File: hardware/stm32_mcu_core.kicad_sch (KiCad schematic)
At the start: 17 parts, among them J4 Conn_ST_STDC14, U5 74AHCT125, U6 STM32G431KBTx, U7 SN74LVC1T45DBV

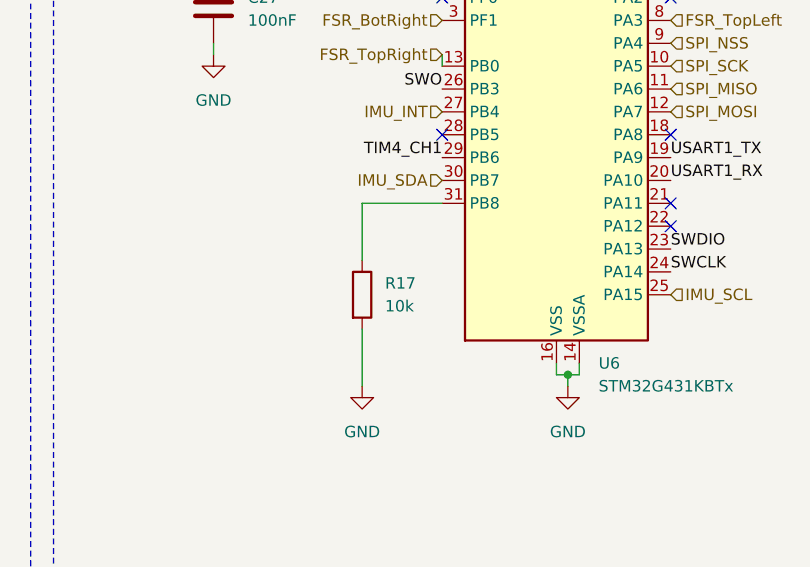
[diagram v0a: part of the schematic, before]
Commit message: Adding power LED status
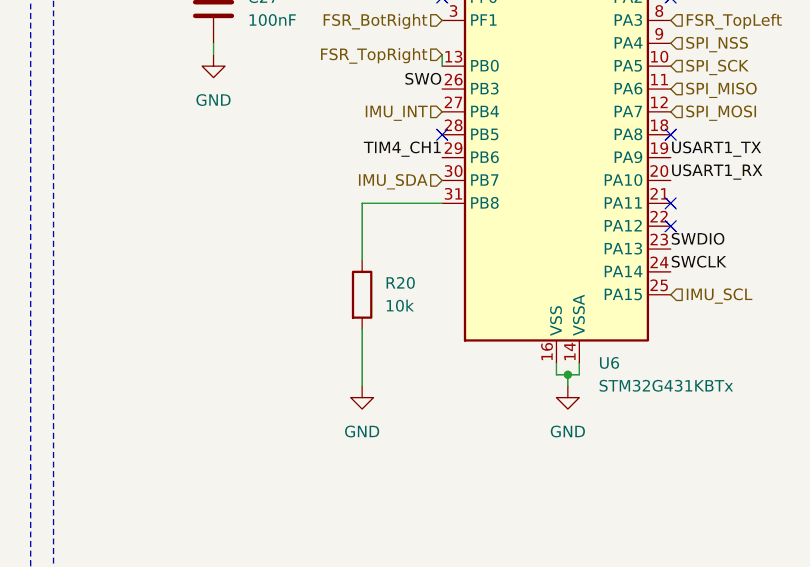
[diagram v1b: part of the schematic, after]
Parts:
- renumbered R17 to R20

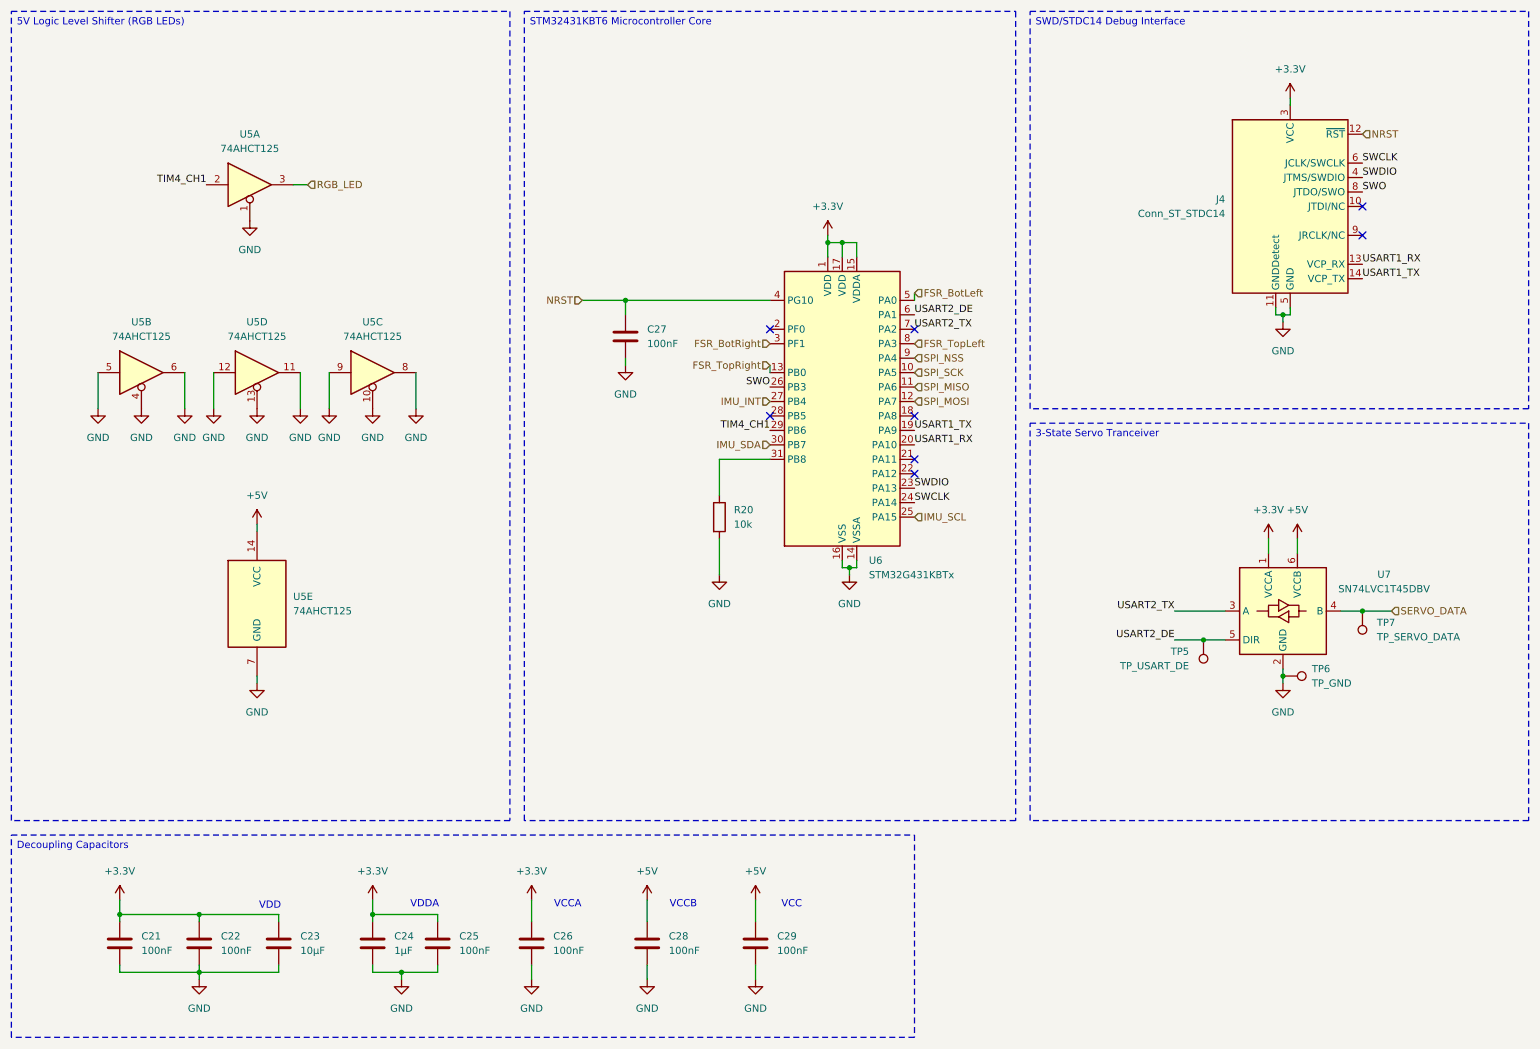
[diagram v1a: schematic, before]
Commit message: Adding footprint & symbol folders
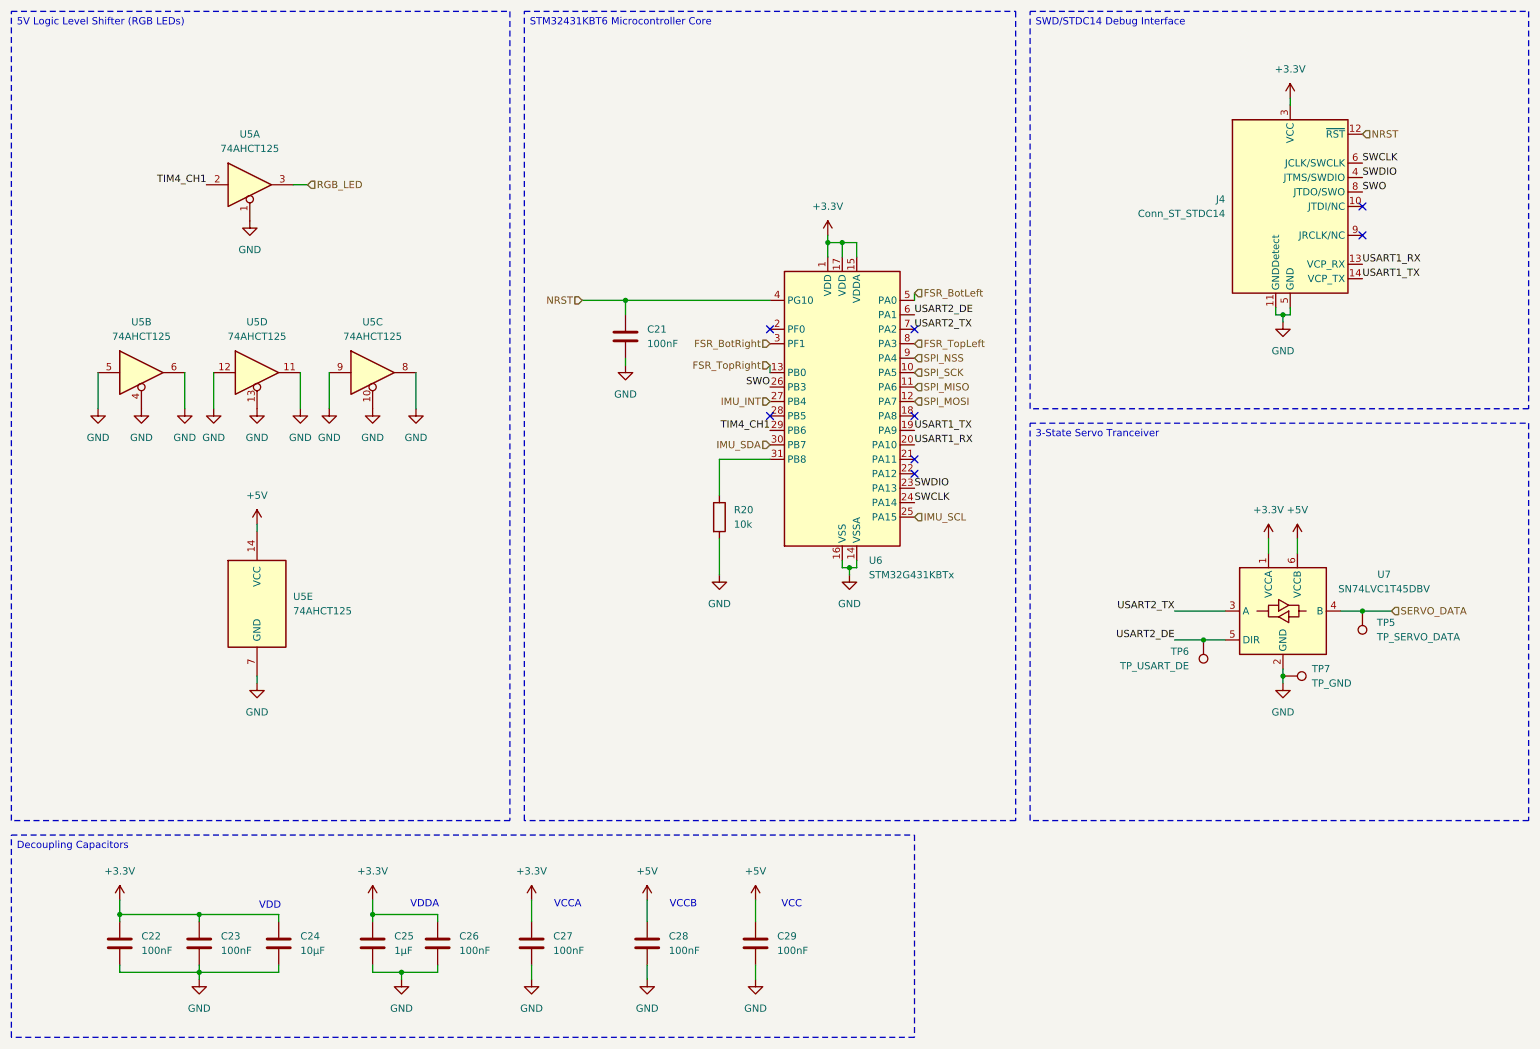
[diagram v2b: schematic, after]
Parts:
- renumbered C27 to C21, C21 to C22, C22 to C23, C23 to C24, C24 to C25, C25 to C26, C26 to C27, TP7 to TP5, TP5 to TP6, TP6 to TP7

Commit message: Adding footprints
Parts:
- J4: footprint (none) -> Chromapi_FP:SAMTEC_FTSH-107-01-L-DV-K-A
- U5: footprint (none) -> Package_SO:TSSOP-14_4.4x5mm_P0.65mm
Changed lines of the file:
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@@
 			)
 		)
-		(property "Footprint" ""
+		(property "Footprint" "Package_SO:TSSOP-14_4.4x5mm_P0.65mm"
 			(at 38.1 78.74 0)
 			(effects
@@
 			)
 		)
-		(property "Footprint" ""
+		(property "Footprint" "Package_SO:TSSOP-14_4.4x5mm_P0.65mm"
 			(at 58.42 78.74 0)
 			(effects
@@
 			)
 		)
-		(property "Footprint" ""
+		(property "Footprint" "Package_SO:TSSOP-14_4.4x5mm_P0.65mm"
 			(at 78.74 78.74 0)
 			(effects
@@
 			)
 		)
-		(property "Footprint" ""
+		(property "Footprint" "Chromapi_FP:SAMTEC_FTSH-107-01-L-DV-K-A"
 			(at 240.03 49.53 0)
 			(effects
@@
 			)
 		)
-		(property "Footprint" ""
+		(property "Footprint" "Package_SO:TSSOP-14_4.4x5mm_P0.65mm"
 			(at 58.42 119.38 0)
 			(effects
@@
 			)
 		)
-		(property "Footprint" ""
+		(property "Footprint" "Package_SO:TSSOP-14_4.4x5mm_P0.65mm"
 			(at 57.15 45.72 0)
 			(effects

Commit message: Updating footprints
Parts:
- C21, C22, C23, C25, C26, C27, C28, C29: footprint (none) -> Capacitor_SMD:C_0603_1608Metric
- C24: footprint (none) -> Capacitor_SMD:C_0805_2012Metric
- R20: footprint (none) -> Capacitor_SMD:C_0201_0603Metric
- TP5, TP6: footprint (none) -> TestPoint:TestPoint_Pad_D1.0mm
- TP7: footprint (none) -> TestPoint:TestPoint_Pad_D1.5mm
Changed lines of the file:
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@@
 			)
 		)
-		(property "Footprint" ""
+		(property "Footprint" "TestPoint:TestPoint_Pad_D1.5mm"
 			(at 238.76 137.16 0)
 			(effects
@@
 			)
 		)
-		(property "Footprint" ""
+		(property "Footprint" "Capacitor_SMD:C_0603_1608Metric"
 			(at 127.9652 182.88 0)
 			(effects
@@
 			)
 		)
-		(property "Footprint" ""
+		(property "Footprint" "Capacitor_SMD:C_0603_1608Metric"
 			(at 107.6452 182.88 0)
 			(effects
@@
 			)
 		)
-		(property "Footprint" ""
+		(property "Footprint" "Capacitor_SMD:C_0603_1608Metric"
 			(at 91.1352 182.88 0)
 			(effects
@@
 			)
 		)
-		(property "Footprint" ""
+		(property "Footprint" "Capacitor_SMD:C_0201_0603Metric"
 			(at 137.922 104.14 90)
 			(effects
@@
 			)
 		)
-		(property "Footprint" ""
+		(property "Footprint" "TestPoint:TestPoint_Pad_D1.0mm"
 			(at 229.87 125.73 0)
 			(effects
@@
 			)
 		)
-		(property "Footprint" ""
+		(property "Footprint" "Capacitor_SMD:C_0603_1608Metric"
 			(at 49.2252 182.88 0)
 			(effects
@@
 			)
 		)
-		(property "Footprint" ""
+		(property "Footprint" "TestPoint:TestPoint_Pad_D1.0mm"
 			(at 247.65 120.65 0)
 			(effects
@@
 			)
 		)
-		(property "Footprint" ""
+		(property "Footprint" "Capacitor_SMD:C_0805_2012Metric"
 			(at 63.1952 182.88 0)
 			(effects
@@
 			)
 		)
-		(property "Footprint" ""
+		(property "Footprint" "Capacitor_SMD:C_0603_1608Metric"
 			(at 79.7052 182.88 0)
 			(effects
@@
 			)
 		)
-		(property "Footprint" ""
+		(property "Footprint" "Capacitor_SMD:C_0603_1608Metric"
 			(at 147.0152 182.88 0)
 			(effects
@@
 			)
 		)
-		(property "Footprint" ""
+		(property "Footprint" "Capacitor_SMD:C_0603_1608Metric"
 			(at 124.1552 76.2 0)
 			(effects
@@
 			)
 		)
-		(property "Footprint" ""
+		(property "Footprint" "Capacitor_SMD:C_0603_1608Metric"
 			(at 35.2552 182.88 0)
 			(effects

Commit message: Modyfing components footprints
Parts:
- C21, C22, C23, C26, C27, C28, C29: footprint Capacitor_SMD:C_0603_1608Metric -> Capacitor_SMD:C_0402_1005Metric
- R20: footprint Capacitor_SMD:C_0201_0603Metric -> Resistor_SMD:R_0402_1005Metric

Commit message: Updating component placement
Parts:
- C24: footprint Capacitor_SMD:C_0805_2012Metric -> Capacitor_SMD:CP_Elec_4x4.5
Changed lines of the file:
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@@
 			)
 		)
-		(property "Footprint" "Capacitor_SMD:C_0805_2012Metric"
+		(property "Footprint" "Capacitor_SMD:CP_Elec_4x4.5"
 			(at 63.1952 182.88 0)
 			(effects

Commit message: Adding some MPN/MPR
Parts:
- J4: MFR (none) -> FTSH-107-01-F-DV-K
- U5: MFR (none) -> SN74AHCT125PWR
- U6: MPN (none) -> STM32G431KBT6
- U7: MPN (none) -> SN74LVC1T45DBVT
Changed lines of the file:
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@@
 			)
 		)
+		(property "MPN" "SN74LVC1T45DBVT"
+			(at 238.76 120.65 0)
+			(effects
+				(font
+					(size 1.27 1.27)
+				)
+				(hide yes)
+			)
+		)
 		(property "Sim.Device" ""
 			(at 238.76 120.65 0)
@@
 			)
 		)
+		(property "MFR" "SN74AHCT125PWR"
+			(at 38.1 78.74 0)
+			(effects
+				(font
+					(size 1.27 1.27)
+				)
+				(hide yes)
+			)
+		)
 		(pin "8"
 		)
@@
 			)
 		)
+		(property "MFR" "SN74AHCT125PWR"
+			(at 58.42 78.74 0)
+			(effects
+				(font
+					(size 1.27 1.27)
+				)
+				(hide yes)
+			)
+		)
 		(property "Sim.Device" ""
 			(at 58.42 78.74 0)
@@
 			)
 		)
+		(property "MFR" "SN74AHCT125PWR"
+			(at 78.74 78.74 0)
+			(effects
+				(font
+					(size 1.27 1.27)
+				)
+				(hide yes)
+			)
+		)
 		(pin "8"
 		)
@@
 			)
 		)
+		(property "MFR" "FTSH-107-01-F-DV-K"
+			(at 240.03 49.53 0)
+			(effects
+				(font
+					(size 1.27 1.27)
+				)
+				(hide yes)
+			)
+		)
 		(property "Sim.Device" ""
 			(at 240.03 49.53 0)
@@
 			)
 		)
+		(property "MFR" "SN74AHCT125PWR"
+			(at 58.42 119.38 0)
+			(effects
+				(font
+					(size 1.27 1.27)
+				)
+				(hide yes)
+			)
+		)
 		(pin "8"
 		)
@@
 			)
 		)
+		(property "MPN" "STM32G431KBT6"
+			(at 161.29 86.36 0)
+			(effects
+				(font
+					(size 1.27 1.27)
+				)
+				(hide yes)
+			)
+		)
 		(property "Sim.Device" ""
 			(at 161.29 86.36 0)
@@
 			(at 57.15 45.72 0)
 			(effects
+				(font
+					(size 1.27 1.27)
+				)
+				(hide yes)
+			)
+		)
+		(property "MFR" "SN74AHCT125PWR"
+			(at 57.15 45.72 0)
+			(effects

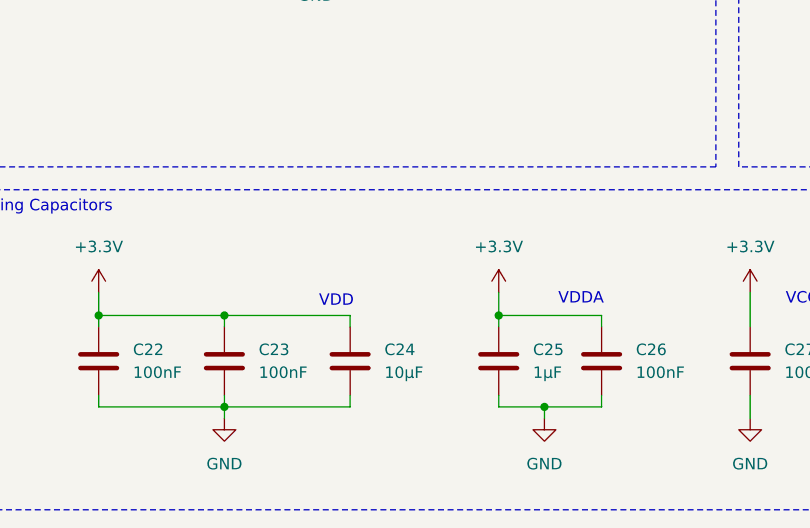
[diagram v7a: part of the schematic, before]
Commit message: Applying first corrections from first review
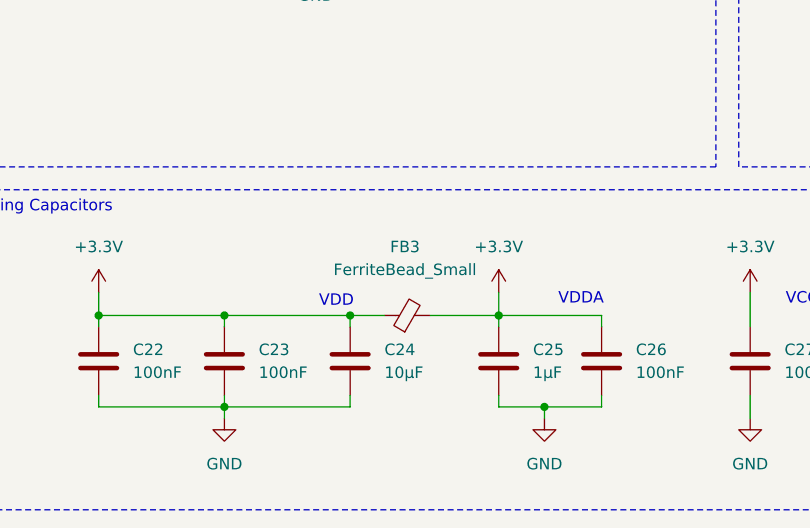
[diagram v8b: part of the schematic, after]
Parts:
- added FB3: FerriteBead_Small, symbol Device:FerriteBead_Small
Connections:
- net +3.3V: now also FB3.1, FB3.2
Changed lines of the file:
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@@
 	)
 	(junction
+		(at 62.23 173.99)
+		(diameter 0)
+		(color 0 0 0 0)
+	)
+	(junction
 		(at 158.75 55.88)
 		(diameter 0)
@@
 	(wire
 		(pts
+			(xy 71.12 173.99) (xy 78.74 173.99)
+		)
+		(stroke
+			(width 0)
+			(type default)
+		)
+	)
+	(wire
+		(pts
 			(xy 148.59 77.47) (xy 148.59 78.74)
 		)
@@
 	(wire
 		(pts
+			(xy 62.23 173.99) (xy 66.04 173.99)
+		)
+		(stroke
+			(width 0)
+			(type default)
+		)
+	)
+	(wire
+		(pts
 			(xy 238.76 132.08) (xy 238.76 133.35)
 		)
@@
 					(unit 1)
 				)
+			)
+		)
+	)
+	(symbol
+		(lib_id "Device:FerriteBead_Small")
+		(at 68.58 173.99 90)
+		(unit 1)
+		(exclude_from_sim no)
+		(in_bom yes)
+		(on_board yes)
+		(dnp no)
+		(property "Reference" "FB3"
+			(at 68.326 166.37 90)
+			(effects
+				(font
+					(size 1.27 1.27)
+				)
+			)
+		)
+		(property "Value" "FerriteBead_Small"
+			(at 68.326 168.91 90)
+			(effects
+				(font
+					(size 1.27 1.27)
+				)
+			)
+		)
+		(property "Footprint" ""
+			(at 68.58 175.768 90)
+			(effects
+				(font
+					(size 1.27 1.27)
+				)
+				(hide yes)
+			)
+		)
+		(property "Datasheet" "~"
+			(at 68.58 173.99 0)
+			(effects
+				(font
+					(size 1.27 1.27)
+				)
+				(hide yes)
+			)
+		)
+		(property "Description" "Ferrite bead, small symbol"
+			(at 68.58 173.99 0)
+			(effects
+				(font
+					(size 1.27 1.27)
+				)
+				(hide yes)
+			)
+		)
+		(pin "2"
+		)
+		(pin "1"
+		)
+		(instances
+			(project ""
+				(path "/d1a31f26-03e0-43e1-89c1-031fe31befc5/bae822f9-c188-4212-9c8c-b50c99d73590"
+					(reference "FB3")
+					(unit 1)
+				)
